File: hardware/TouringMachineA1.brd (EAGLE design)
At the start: 30.2 x 106.5 mm, 62 parts, among them IC1 78L05F, J1 PJ301_THONKICONN6, J2 PJ301_THONKICONN6, J3 PJ301_THONKICONN6, J4 PJ301_THONKICONN6, U1 MCP6002_, U2 TL072_SMD

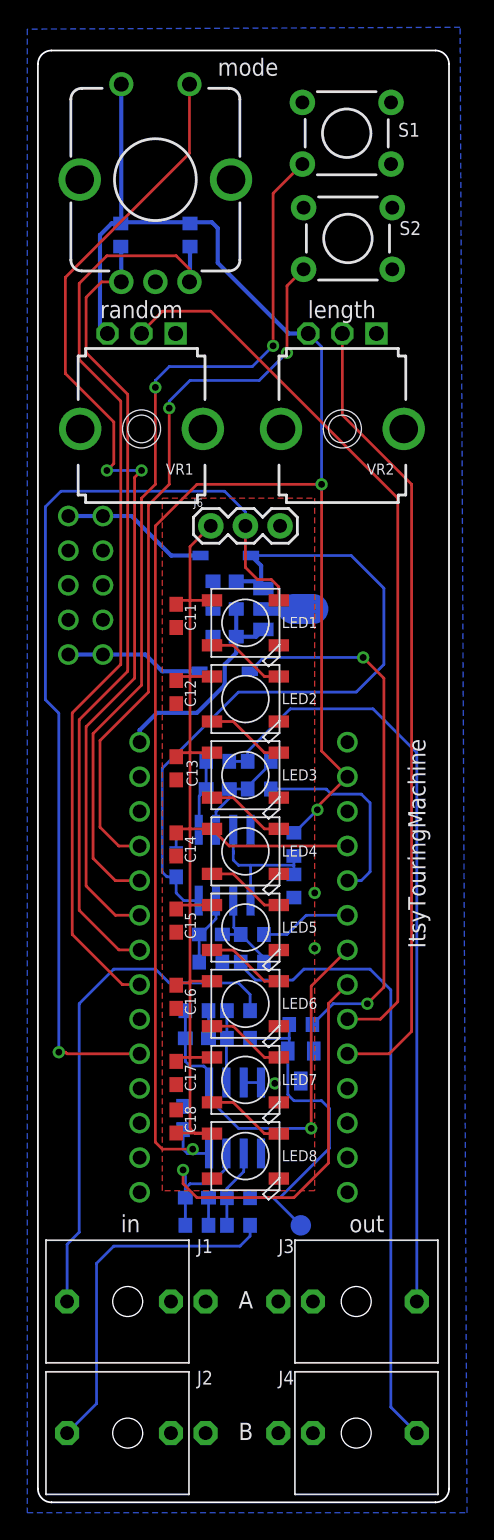
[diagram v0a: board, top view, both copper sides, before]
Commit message: added 3d models
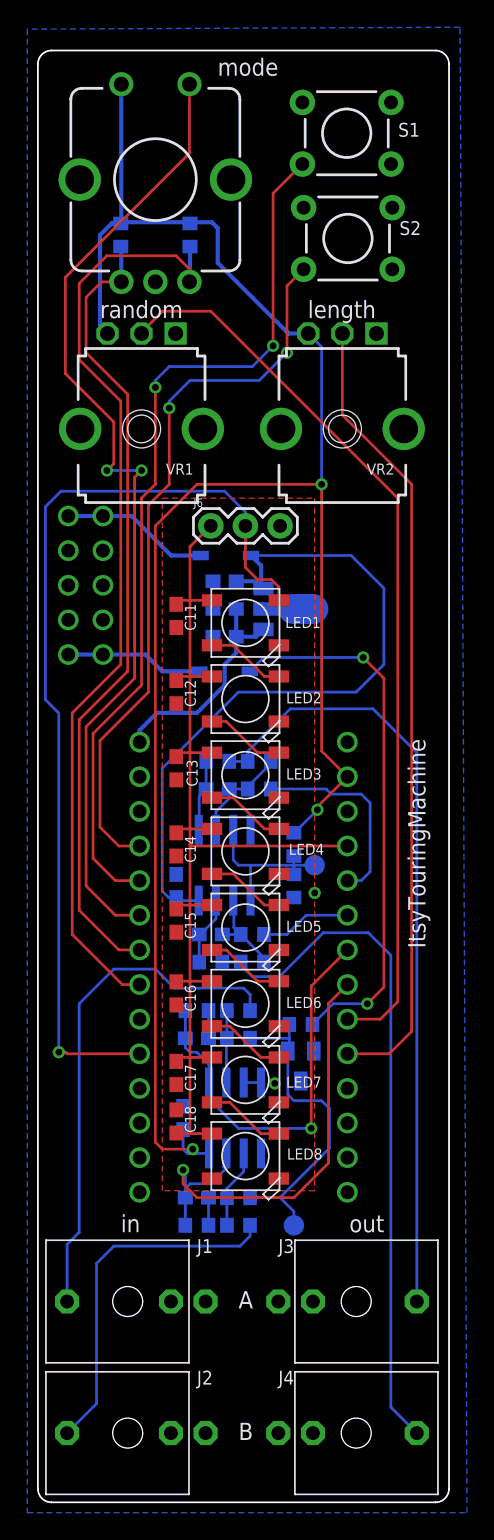
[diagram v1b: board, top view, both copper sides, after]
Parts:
- added TP2: TPTP15R, testpad:TP15R
- moved C9 1.52 mm to (10.2, 45.2)
- moved TP1 0.51 mm to (18.8, 20.3)
- moved C16 0.25 mm to (10.2, 37.3)
- renumbered U$2 to J5
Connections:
- net VREF_MID: now also TP2.TP
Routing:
- net CVB_OUT_JACK: track 47.3 -> 50.8 mm
- net VREF_-10: track 26.3 -> 24.2 mm
- net GND: track 2.96 -> 1.27 mm, vias 3 -> 2
- net VREF_MID: track 10.8 -> 12.3 mm
- net CVA_IN: track 30.4 -> 30.9 mm
